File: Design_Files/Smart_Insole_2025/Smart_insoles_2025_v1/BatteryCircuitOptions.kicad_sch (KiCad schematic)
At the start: 23 parts, among them J3 S2B-PH-SM4-TB_LF__SN_, Q2 FDN306P, U1 ME6211C33M5, U5 BQ24040DSQR

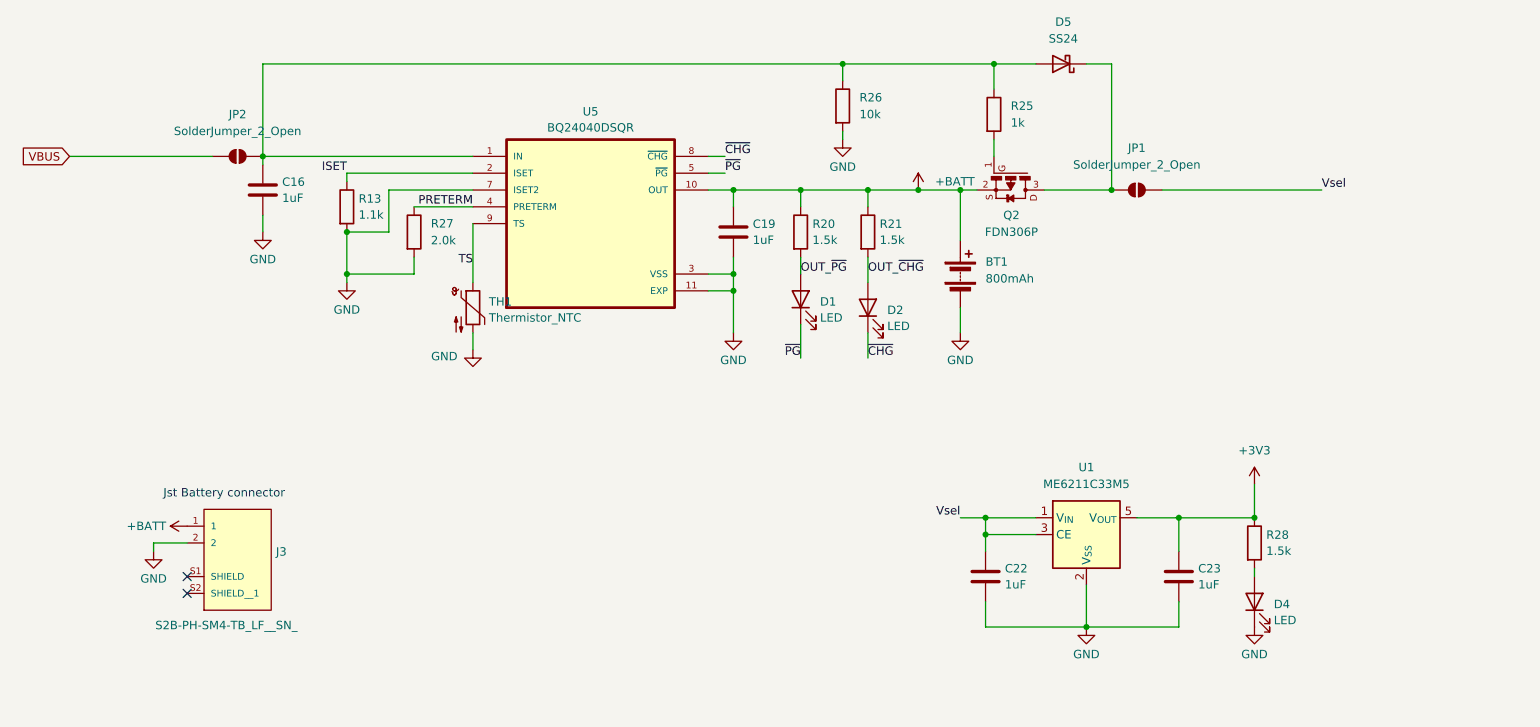
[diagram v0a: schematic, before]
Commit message: SCH:Solved Errors in ERC
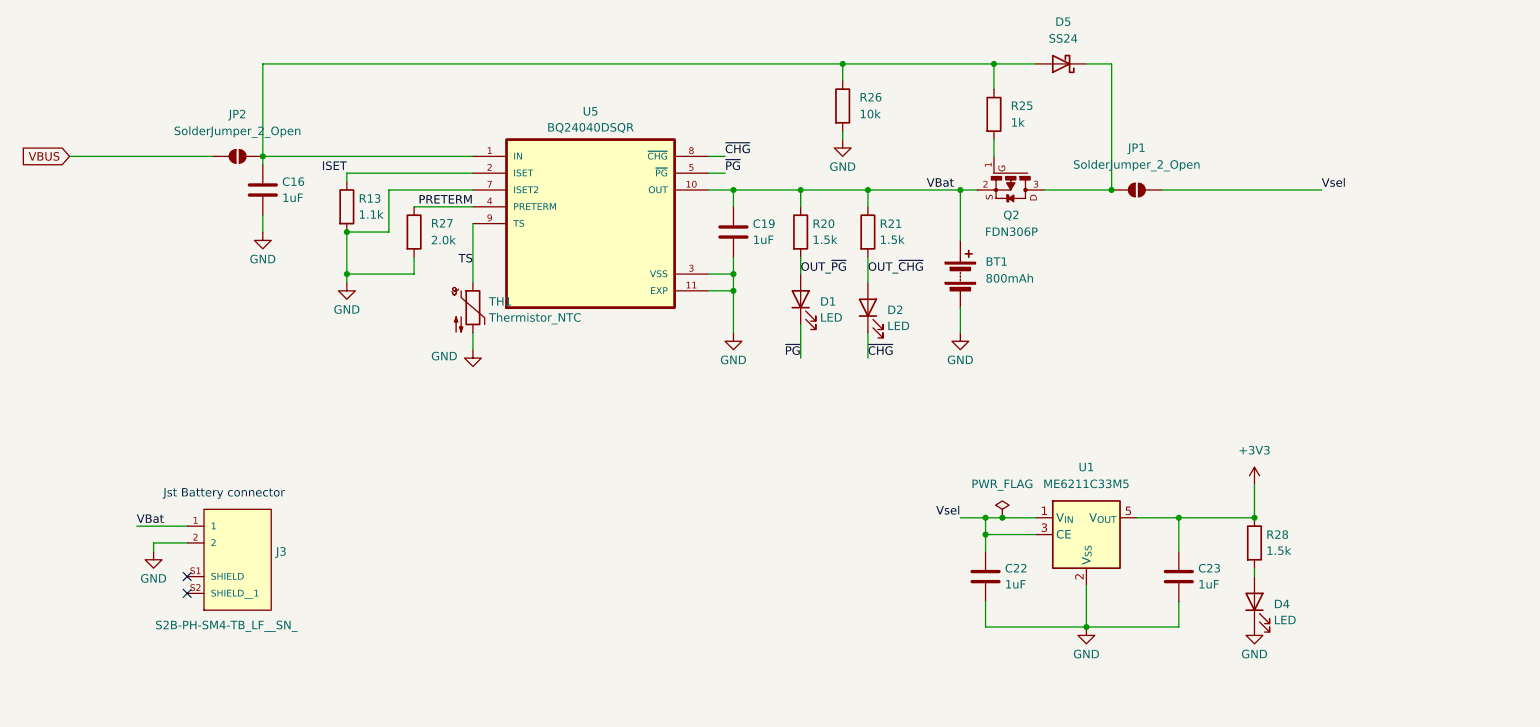
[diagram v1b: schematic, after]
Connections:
- net +BATT renamed VBat
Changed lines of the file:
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@@
 	)
 	(junction
+		(at 177.8 105.41)
+		(diameter 0)
+		(color 0 0 0 0)
+	)
+	(junction
 		(at 66.04 50.8)
 		(diameter 0)
@@
 		(color 0 0 0 0)
 	)
-	(junction
-		(at 165.1 55.88)
-		(diameter 0)
-		(color 0 0 0 0)
-	)
 	(no_connect
 		(at 54.61 114.3)
@@
 	(wire
 		(pts
+			(xy 46.99 106.68) (xy 54.61 106.68)
+		)
+		(stroke
+			(width 0)
+			(type default)
+		)
+	)
+	(wire
+		(pts
 			(xy 171.45 55.88) (xy 171.45 63.5)
 		)
@@
 	(wire
 		(pts
-			(xy 49.53 110.49) (xy 49.53 109.22)
+			(xy 177.8 105.41) (xy 175.26 105.41)
 		)
 		(stroke
@@
 	(wire
 		(pts
-			(xy 175.26 107.95) (xy 175.26 110.49)
+			(xy 49.53 110.49) (xy 49.53 109.22)
 		)
 		(stroke
@@
 	(wire
 		(pts
-			(xy 135.89 53.34) (xy 133.35 53.34)
+			(xy 175.26 107.95) (xy 175.26 110.49)
 		)
 		(stroke
@@
 	(wire
 		(pts
-			(xy 175.26 107.95) (xy 182.88 107.95)
+			(xy 135.89 53.34) (xy 133.35 53.34)
 		)
 		(stroke
@@
 	(wire
 		(pts
-			(xy 165.1 55.88) (xy 171.45 55.88)
+			(xy 175.26 107.95) (xy 182.88 107.95)
 		)
 		(stroke
@@
 	(wire
 		(pts
-			(xy 182.88 105.41) (xy 175.26 105.41)
+			(xy 182.88 105.41) (xy 177.8 105.41)
 		)
 		(stroke
@@
 	(wire
 		(pts
-			(xy 165.1 55.88) (xy 157.48 55.88)
+			(xy 157.48 55.88) (xy 171.45 55.88)
 		)
 		(stroke
@@
 		)
 	)
+	(label "VBat"
+		(at 166.37 55.88 0)
+		(effects
+			(font
+				(size 1.27 1.27)
+			)
+			(justify left bottom)
+		)
+	)
 	(label "PRETERM"
 		(at 97.79 58.42 180)
@@
 		)
 	)
+	(label "VBat"
+		(at 46.99 106.68 0)
+		(effects
+			(font
+				(size 1.27 1.27)
+			)
+			(justify left bottom)
+		)
+	)
 	(label "~{CHG}"
 		(at 157.48 81.28 0)
@@
 	)
 	(symbol
-		(lib_id "power:+BATT")
-		(at 54.61 106.68 90)
-		(unit 1)
-		(exclude_from_sim no)
-		(in_bom yes)
-		(on_board yes)
-		(dnp no)
-		(fields_autoplaced yes)
-		(property "Reference" "#PWR022"
-			(at 58.42 106.68 0)
-			(effects
-				(font
-					(size 1.27 1.27)
-				)
-				(hide yes)
-			)
-		)
-		(property "Value" "+BATT"
-			(at 51.435 106.68 90)
-			(effects
-				(font
-					(size 1.27 1.27)
-				)
-				(justify left)
-			)
-		)
-		(property "Footprint" ""
-			(at 54.61 106.68 0)
-			(effects
-				(font
-					(size 1.27 1.27)
-				)
-				(hide yes)
-			)
-		)
-		(property "Datasheet" ""
-			(at 54.61 106.68 0)
-			(effects
-				(font
-					(size 1.27 1.27)
-				)
-				(hide yes)
-			)
-		)
-		(property "Description" "Power symbol creates a global label with name \"+BATT\""
-			(at 54.61 106.68 0)
-			(effects
-				(font
-					(size 1.27 1.27)
-				)
-				(hide yes)
-			)
-		)
-		(pin "1"
-		)
-		(instances
-			(project "Smart_insoles_2025_v1"
-				(path "/f1f3d712-154d-4111-a7c4-f47541abccf8/720d2e8f-49b8-46ab-8d82-07d24ffc5c73"
-					(reference "#PWR022")
-					(unit 1)
-				)
-			)
-		)
-	)
-	(symbol
 		(lib_id "Device:C")
 		(at 175.26 114.3 180)
@@
 	)
 	(symbol
-		(lib_id "power:+BATT")
-		(at 165.1 55.88 0)
-		(unit 1)
-		(exclude_from_sim no)
-		(in_bom yes)
-		(on_board yes)
-		(dnp no)
-		(fields_autoplaced yes)
-		(property "Reference" "#PWR042"
-			(at 165.1 59.69 0)
-			(effects
-				(font
-					(size 1.27 1.27)
-				)
-				(hide yes)
-			)
-		)
-		(property "Value" "+BATT"
-			(at 167.64 54.6099 0)
-			(effects
-				(font
-					(size 1.27 1.27)
-				)
-				(justify left)
-			)
-		)
-		(property "Footprint" ""
-			(at 165.1 55.88 0)
-			(effects
-				(font
-					(size 1.27 1.27)
-				)
-				(hide yes)
-			)
-		)
-		(property "Datasheet" ""
-			(at 165.1 55.88 0)
-			(effects
-				(font
-					(size 1.27 1.27)
-				)
-				(hide yes)
-			)
-		)
-		(property "Description" "Power symbol creates a global label with name \"+BATT\""
-			(at 165.1 55.88 0)
-			(effects
-				(font
-					(size 1.27 1.27)
-				)
-				(hide yes)
-			)
-		)
-		(pin "1"
-		)
-		(instances
-			(project "Smart_insoles_2025_v1"
-				(path "/f1f3d712-154d-4111-a7c4-f47541abccf8/720d2e8f-49b8-46ab-8d82-07d24ffc5c73"
-					(reference "#PWR042")
-					(unit 1)
-				)
-			)
-		)
-	)
-	(symbol
 		(lib_id "Device:R")
 		(at 147.32 62.23 0)
@@
 					(unit 1)
 				)
+			)
+		)
+	)
+	(symbol
+		(lib_id "power:PWR_FLAG")
+		(at 177.8 105.41 0)
+		(unit 1)
+		(exclude_from_sim no)
+		(in_bom yes)
+		(on_board yes)
+		(dnp no)
+		(fields_autoplaced yes)
+		(property "Reference" "#FLG01"
+			(at 177.8 103.505 0)
+			(effects
+				(font
+					(size 1.27 1.27)
+				)
+				(hide yes)
+			)
+		)
+		(property "Value" "PWR_FLAG"
+			(at 177.8 100.33 0)
+			(effects
+				(font
+					(size 1.27 1.27)
+				)
+			)
+		)
+		(property "Footprint" ""
+			(at 177.8 105.41 0)
+			(effects
+				(font
+					(size 1.27 1.27)
+				)
+				(hide yes)
+			)
+		)
+		(property "Datasheet" "~"
+			(at 177.8 105.41 0)
+			(effects
+				(font
+					(size 1.27 1.27)
+				)
+				(hide yes)
+			)
+		)
+		(property "Description" "Special symbol for telling ERC where power comes from"
+			(at 177.8 105.41 0)
+			(effects
+				(font
+					(size 1.27 1.27)
+				)
+				(hide yes)
+			)
+		)
+		(pin "1"
+		)
+		(instances
+			(project ""
+				(path "/f1f3d712-154d-4111-a7c4-f47541abccf8/720d2e8f-49b8-46ab-8d82-07d24ffc5c73"
+					(reference "#FLG01")
+					(unit 1)
+				)

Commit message: SCH: Added missing footprints. PCB: Grouped related components for new layout
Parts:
- C16, C19, C22, C23: footprint Capacitor_SMD:C_0603_1608Metric -> Capacitor_SMD:C_0805_2012Metric_Pad1.18x1.45mm_HandSolder
- JP1: footprint (none) -> Capacitor_SMD:C_0805_2012Metric
- JP2, R25, R26: footprint (none) -> Capacitor_SMD:C_0805_2012Metric_Pad1.18x1.45mm_HandSolder
- TH1: footprint (none) -> Connector_JST:JST_ACH_BM02B-ACHSS-GAN-ETF_1x02-1MP_P1.20mm_Vertical
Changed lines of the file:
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@@
 			)
 		)
-		(property "Footprint" "Capacitor_SMD:C_0603_1608Metric"
+		(property "Footprint" "Capacitor_SMD:C_0805_2012Metric_Pad1.18x1.45mm_HandSolder"
 			(at 174.2948 110.49 0)
 			(effects
@@
 			)
 		)
-		(property "Footprint" ""
+		(property "Footprint" "Capacitor_SMD:C_0805_2012Metric"
 			(at 198.12 55.88 0)
 			(effects
@@
 			)
 		)
-		(property "Footprint" "Capacitor_SMD:C_0603_1608Metric"
+		(property "Footprint" "Capacitor_SMD:C_0805_2012Metric_Pad1.18x1.45mm_HandSolder"
 			(at 65.0748 52.07 0)
 			(effects
@@
 			)
 		)
-		(property "Footprint" "Capacitor_SMD:C_0603_1608Metric"
+		(property "Footprint" "Capacitor_SMD:C_0805_2012Metric_Pad1.18x1.45mm_HandSolder"
 			(at 203.5048 110.49 0)
 			(effects
@@
 			)
 		)
-		(property "Footprint" ""
+		(property "Footprint" "Capacitor_SMD:C_0805_2012Metric_Pad1.18x1.45mm_HandSolder"
 			(at 174.752 44.45 90)
 			(effects
@@
 			)
 		)
-		(property "Footprint" ""
+		(property "Footprint" "Capacitor_SMD:C_0805_2012Metric_Pad1.18x1.45mm_HandSolder"
 			(at 62.23 50.8 0)
 			(effects
@@
 			)
 		)
-		(property "Footprint" ""
+		(property "Footprint" "Connector_JST:JST_ACH_BM02B-ACHSS-GAN-ETF_1x02-1MP_P1.20mm_Vertical"
 			(at 97.79 72.39 0)
 			(effects
@@
 			)
 		)
-		(property "Footprint" ""
+		(property "Footprint" "Capacitor_SMD:C_0805_2012Metric_Pad1.18x1.45mm_HandSolder"
 			(at 151.892 43.18 90)
 			(effects
@@
 			)
 		)
+		(property "3D Model" ""
+			(at 115.57 60.96 0)
+			(effects
+				(font
+					(size 1.27 1.27)
+				)
+				(hide yes)
+			)
+		)
+		(property "LCSC MANUFACTURER" ""
+			(at 115.57 60.96 0)
+			(effects
+				(font
+					(size 1.27 1.27)
+				)
+				(hide yes)
+			)
+		)
 		(pin "5"
 		)
@@
 			)
 		)
-		(property "Footprint" "Capacitor_SMD:C_0603_1608Metric"
+		(property "Footprint" "Capacitor_SMD:C_0805_2012Metric_Pad1.18x1.45mm_HandSolder"
 			(at 136.1948 58.42 0)
 			(effects

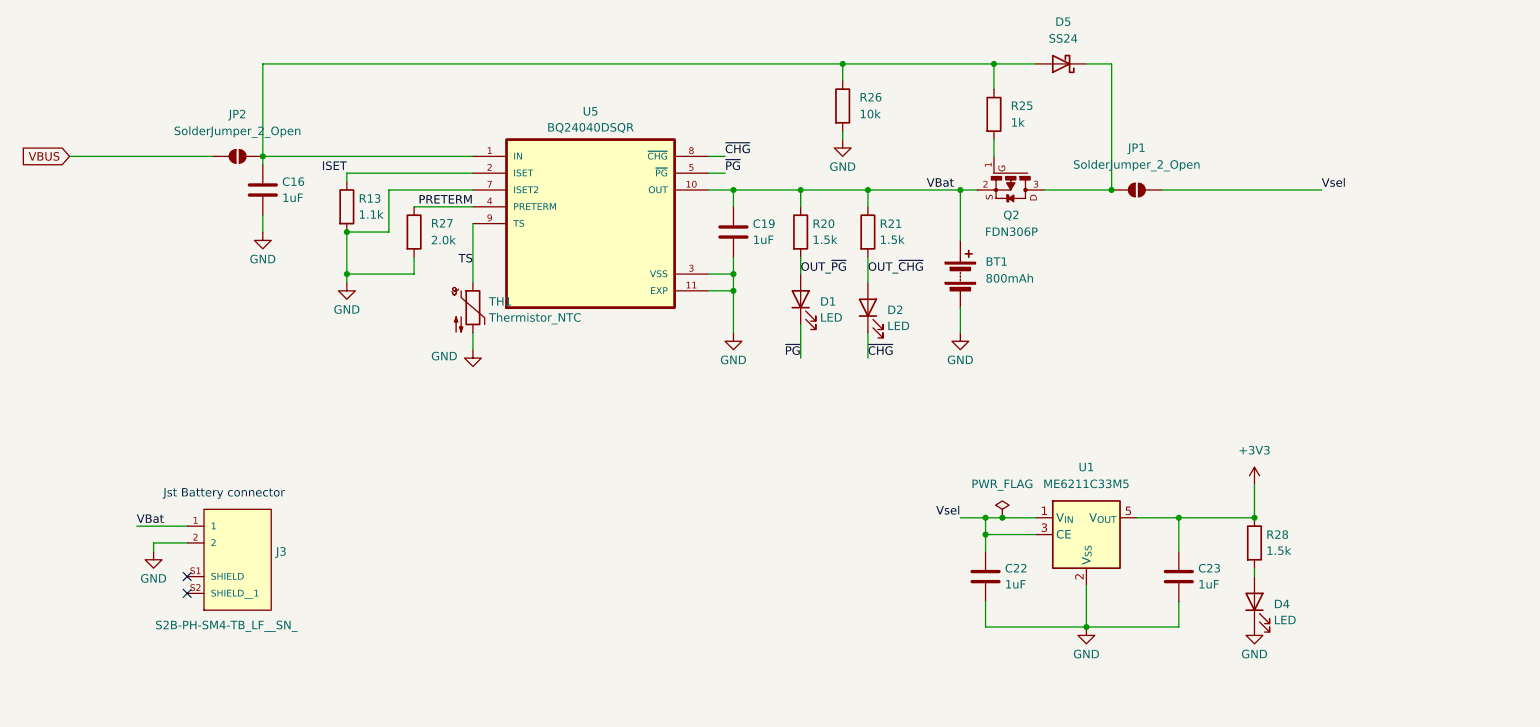
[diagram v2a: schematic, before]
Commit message: SCH: Fixed Warnings. Added thermistor solder pads library.
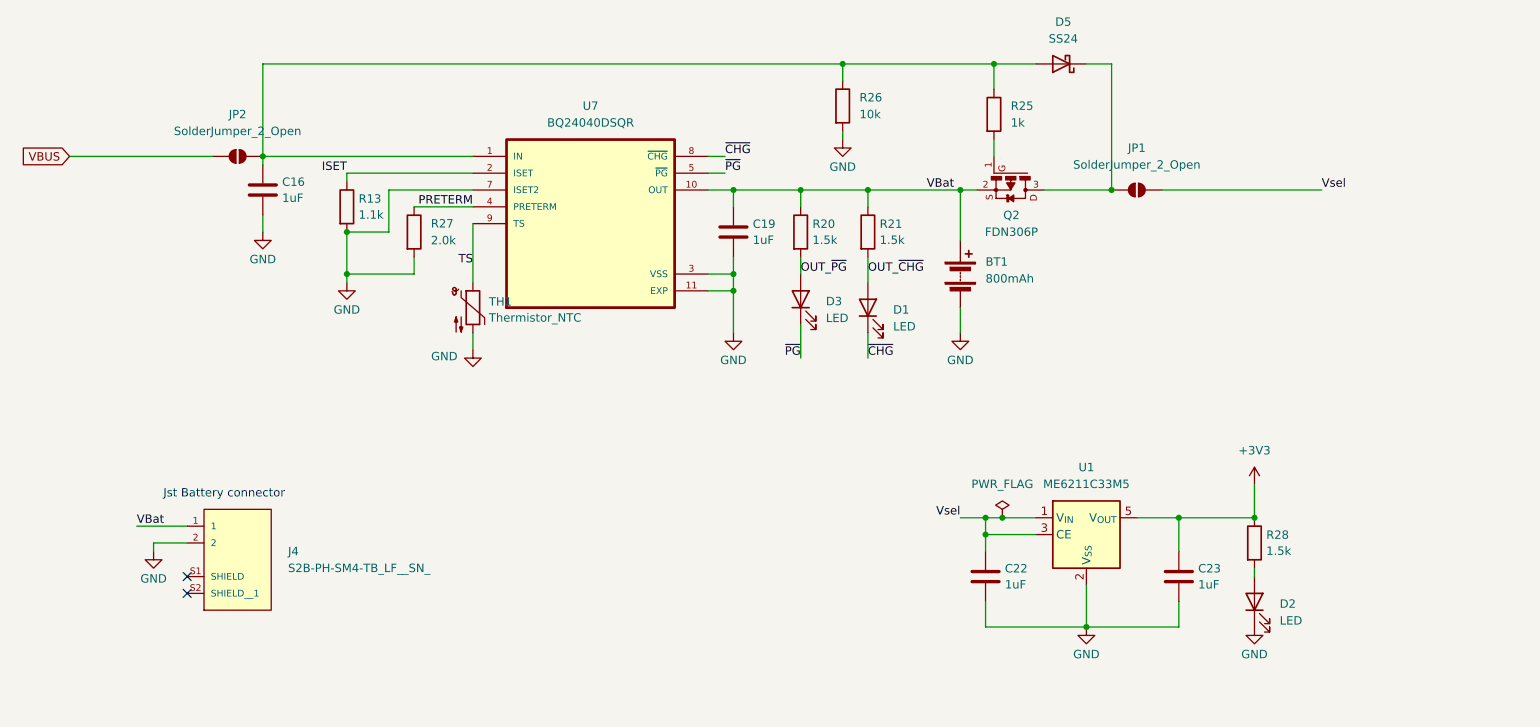
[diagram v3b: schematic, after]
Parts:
- removed D4: LED, LED_SMD:LED_0603_1608Metric, symbol Device:LED
- removed J3: S2B-PH-SM4-TB_LF__SN_, JST-PH2-2.00MM-SMD-HORIZONTAL:JST_S2B-PH-SM4-TB_LF__SN_, symbol S2B-PH-SM4-TB_LF__SN_:S2B-PH-SM4-TB_LF__SN_
- removed U5: BQ24040DSQR, BQ24040DSQR:SON40P200X200X80-11N, symbol BQ24040DSQR:BQ24040DSQR
- added D3: LED, LED_SMD:LED_0805_2012Metric, symbol Device:LED
- added J4: S2B-PH-SM4-TB_LF__SN_, JST-PH2-2.00MM-SMD-HORIZONTAL:JST_S2B-PH-SM4-TB_LF__SN_, symbol S2B-PH-SM4-TB_LF__SN_:S2B-PH-SM4-TB_LF__SN_
- added U7: BQ24040DSQR, BQ24040DSQR:SON40P200X200X80-11N, symbol BQ24040DSQR:BQ24040DSQR
- D1, D2: footprint LED_SMD:LED_0603_1608Metric -> LED_SMD:LED_0805_2012Metric
- JP1: footprint Capacitor_SMD:C_0805_2012Metric -> Jumper:SolderJumper-2_P1.3mm_Open_RoundedPad1.0x1.5mm
- JP2: footprint Capacitor_SMD:C_0805_2012Metric_Pad1.18x1.45mm_HandSolder -> Jumper:SolderJumper-2_P1.3mm_Open_RoundedPad1.0x1.5mm
- R13, R20, R21, R27, R28: footprint Resistor_SMD:R_0603_1608Metric -> Resistor_SMD:R_0805_2012Metric_Pad1.20x1.40mm_HandSolder
- R25, R26: footprint Capacitor_SMD:C_0805_2012Metric_Pad1.18x1.45mm_HandSolder -> Resistor_SMD:R_0805_2012Metric_Pad1.20x1.40mm_HandSolder
- TH1: footprint Connector_JST:JST_ACH_BM02B-ACHSS-GAN-ETF_1x02-1MP_P1.20mm_Vertical -> thermistor_10k_NTC_solderPad:thermistor_10k_NTC_SolderPad
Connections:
- net GND: now also D2.1 (K), J4.2, U7.11 (EXP), U7.3 (VSS), U7.7 (ISET2)
- net ISET: now also U7.2 (ISET)
- net OUT_~{CHG}: now also D1.2 (A); no longer D2.2 (A)
- net OUT_~{PG}: now also D3.2 (A); no longer D1.2 (A)
- net PRETERM: now also U7.4 (PRETERM)
- net TS: now also U7.9 (TS)
- net VBat: now also J4.1, U7.10 (OUT)
- net ~{CHG}: now also D1.1 (K), U7.8 (~{CHG}); no longer D2.1 (K)
- net ~{PG}: now also D3.1 (K), U7.5 (~{PG}); no longer D1.1 (K)
- net at C16.2, D5.2 (A), JP2.2 (B)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: now also U7.1 (IN)
- net at R28.2: now also D2.2 (A)

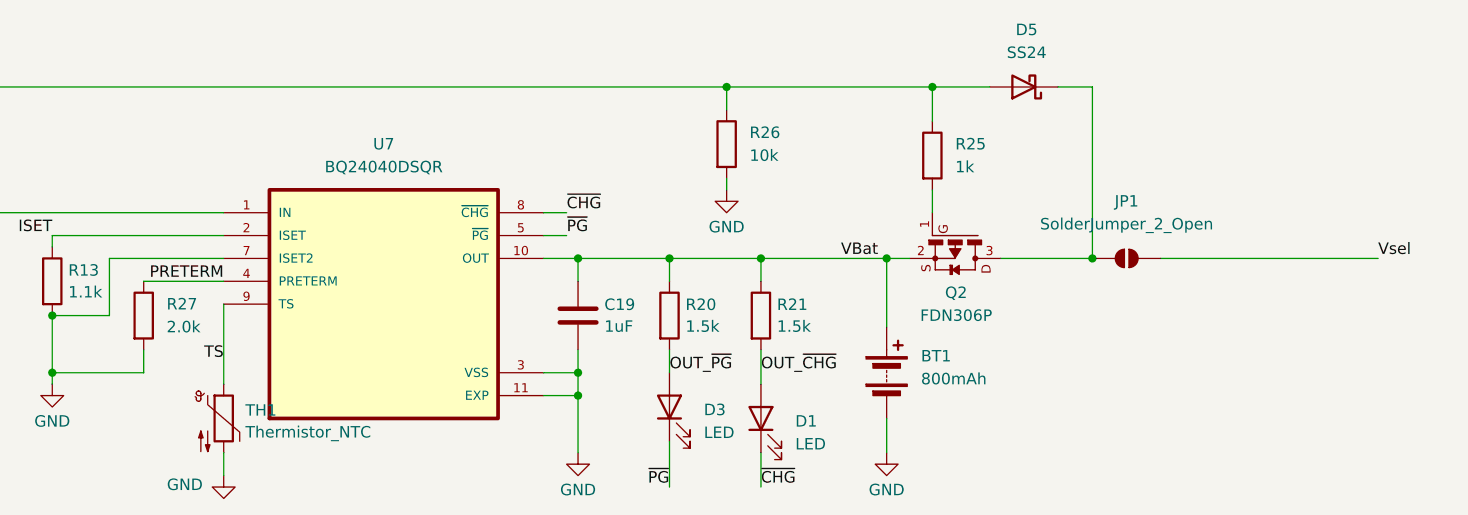
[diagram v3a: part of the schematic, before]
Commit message: SCH: Added Power Test points and Mounting Holes. PCB: Arranged grouped  Footprints to minimize rounting
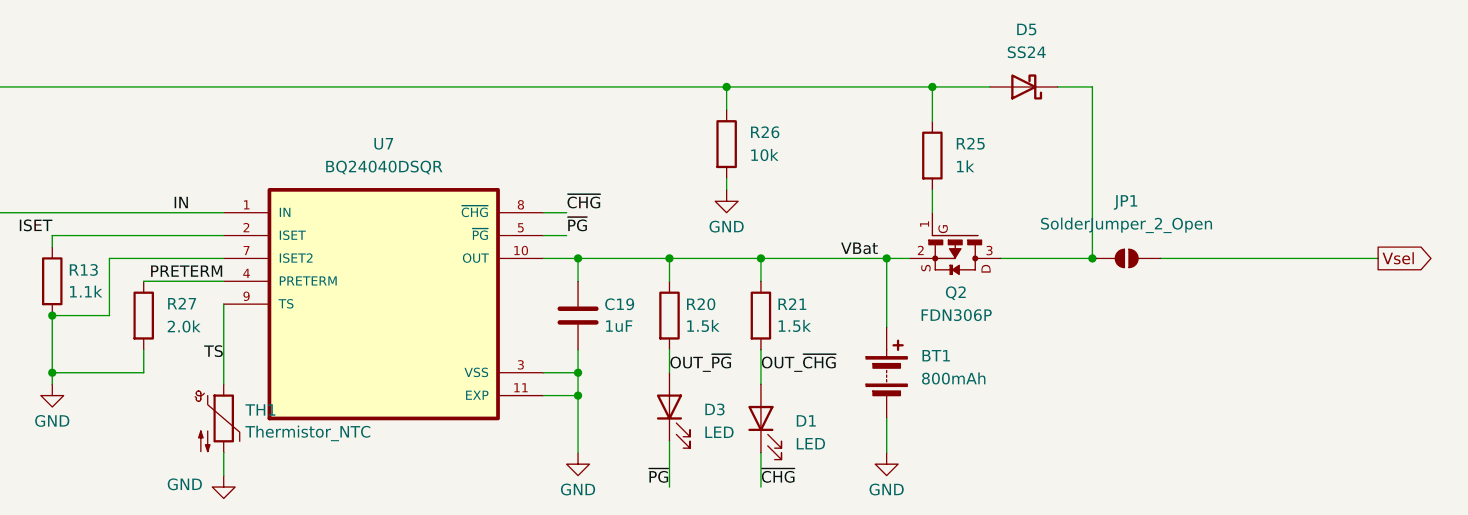
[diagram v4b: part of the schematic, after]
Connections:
- net IN: now reaches C16.2, D5.2 (A), JP2.2 (B), R25.1, R26.1, U7.1 (IN)
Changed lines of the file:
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@@
-		)
-	)
-	(label "Vsel"
-		(at 226.06 55.88 0)
-		(effects
-			(font
-				(size 1.27 1.27)
-			)
-			(justify left bottom)
 		)
 	)
@@
 		)
 	)
+	(label "IN"
+		(at 93.98 50.8 180)
+		(effects
+			(font
+				(size 1.27 1.27)
+			)
+			(justify right bottom)
+		)
+	)
+	(global_label "Vsel"
+		(shape output)
+		(at 226.06 55.88 0)
+		(fields_autoplaced yes)
+		(effects
+			(font
+				(size 1.27 1.27)
+			)
+			(justify left)
+		)
+		(property "Intersheetrefs" "${INTERSHEET_REFS}"
+			(at 232.9157 55.88 0)
+			(effects
+				(font
+					(size 1.27 1.27)
+				)
+				(justify left)
+				(hide yes)
+			)
+		)
+	)
